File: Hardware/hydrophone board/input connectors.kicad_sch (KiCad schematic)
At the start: 9 parts, among them J202 Conn_01x02_Socket, J203 Screw_Terminal_01x02, J205 Conn_01x02_Socket, J207 Conn_01x02_Socket, J209 Conn_01x02_Socket

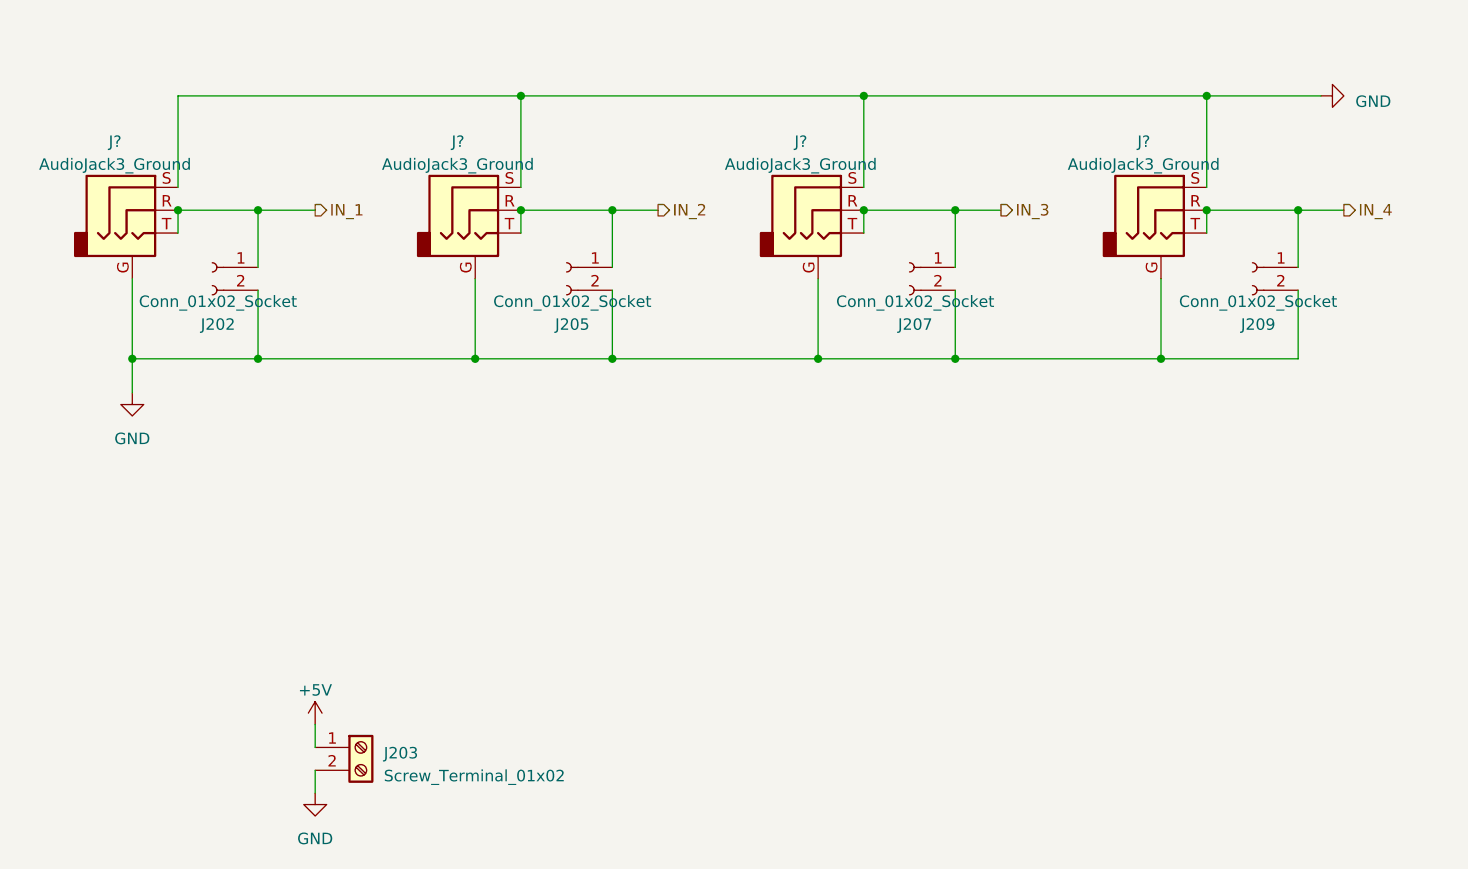
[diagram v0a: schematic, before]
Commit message: added teensy footprint
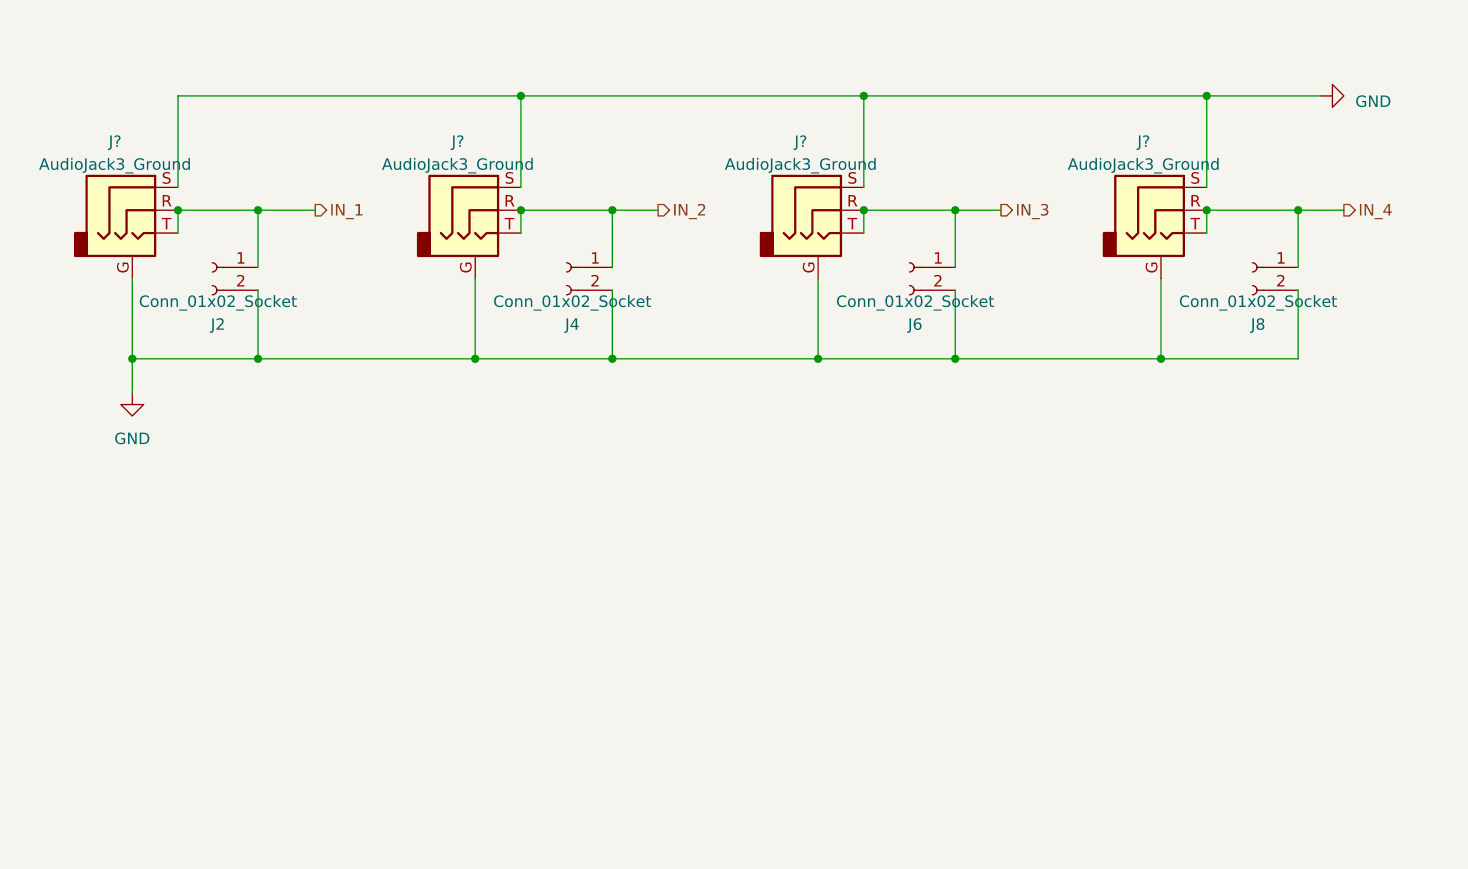
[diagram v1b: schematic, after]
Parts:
- removed J203: Screw_Terminal_01x02, symbol Connector:Screw_Terminal_01x02
- renumbered J202 to J2, J205 to J4, J207 to J6, J209 to J8
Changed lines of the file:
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@@
-    (stroke (width 0) (type default))
-  )
-  (wire (pts (xy 76.2 127) (xy 76.2 129.54))
     (stroke (width 0) (type default))
   )
@@
   )
   (wire (pts (xy 60.96 69.85) (xy 60.96 72.39))
-    (stroke (width 0) (type default))
-  )
-  (wire (pts (xy 76.2 132.08) (xy 76.2 134.62))
     (stroke (width 0) (type default))
   )
@@
         )
         (path "/4356d3a6-6a00-447d-897e-473f60221539/1cfbaf71-7039-4355-8fc7-d8c77f0e8058"
-          (reference "J201") (unit 1)
+          (reference "J1") (unit 1)
         )
       )
@@
   (symbol (lib_id "Connector:Conn_01x02_Socket") (at 180.34 76.2 0) (mirror y) (unit 1)
     (in_bom yes) (on_board yes) (dnp no)
-    (property "Reference" "J209" (at 180.975 82.55 0)
+    (property "Reference" "J8" (at 180.975 82.55 0)
       (effects (font (size 1.27 1.27)))
     )
@@
       (project "hydrophone board"
         (path "/4356d3a6-6a00-447d-897e-473f60221539/1cfbaf71-7039-4355-8fc7-d8c77f0e8058"
-          (reference "J209") (unit 1)
+          (reference "J8") (unit 1)
         )
       )
@@
         )
         (path "/4356d3a6-6a00-447d-897e-473f60221539/1cfbaf71-7039-4355-8fc7-d8c77f0e8058"
-          (reference "J204") (unit 1)
+          (reference "J3") (unit 1)
         )
       )
@@
   (symbol (lib_id "Connector:Conn_01x02_Socket") (at 142.24 76.2 0) (mirror y) (unit 1)
     (in_bom yes) (on_board yes) (dnp no)
-    (property "Reference" "J207" (at 142.875 82.55 0)
+    (property "Reference" "J6" (at 142.875 82.55 0)
       (effects (font (size 1.27 1.27)))
     )
@@
       (project "hydrophone board"
         (path "/4356d3a6-6a00-447d-897e-473f60221539/1cfbaf71-7039-4355-8fc7-d8c77f0e8058"
-          (reference "J207") (unit 1)
+          (reference "J6") (unit 1)
         )
       )
@@
         )
         (path "/4356d3a6-6a00-447d-897e-473f60221539/1cfbaf71-7039-4355-8fc7-d8c77f0e8058"
-          (reference "J206") (unit 1)
+          (reference "J5") (unit 1)
         )
       )
@@
   (symbol (lib_id "power:GND") (at 187.96 57.15 90) (unit 1)
     (in_bom yes) (on_board yes) (dnp no) (fields_autoplaced)
-    (property "Reference" "#PWR0203" (at 194.31 57.15 0)
+    (property "Reference" "#PWR02" (at 194.31 57.15 0)
       (effects (font (size 1.27 1.27)) hide)
     )
@@
       (project "hydrophone board"
         (path "/4356d3a6-6a00-447d-897e-473f60221539/1cfbaf71-7039-4355-8fc7-d8c77f0e8058"
-          (reference "#PWR0203") (unit 1)
-        )
-      )
-    )
-  )
-  (symbol (lib_id "Connector:Screw_Terminal_01x02") (at 81.28 129.54 0) (unit 1)
-    (in_bom yes) (on_board yes) (dnp no) (fields_autoplaced)
-    (property "Reference" "J203" (at 83.82 130.175 0)
-      (effects (font (size 1.27 1.27)) (justify left))
-    )
-    (property "Value" "Screw_Terminal_01x02" (at 83.82 132.715 0)
-      (effects (font (size 1.27 1.27)) (justify left))
-    )
-    (property "Footprint" "" (at 81.28 129.54 0)
-      (effects (font (size 1.27 1.27)) hide)
-    )
-    (property "Datasheet" "~" (at 81.28 129.54 0)
-      (effects (font (size 1.27 1.27)) hide)
-    )
-    (pin "1")
-    (pin "2")
-    (instances
-      (project "hydrophone board"
-        (path "/4356d3a6-6a00-447d-897e-473f60221539/1cfbaf71-7039-4355-8fc7-d8c77f0e8058"
-          (reference "J203") (unit 1)
-        )
-      )
-    )
-  )
-  (symbol (lib_id "power:GND") (at 76.2 134.62 0) (unit 1)
-    (in_bom yes) (on_board yes) (dnp no) (fields_autoplaced)
-    (property "Reference" "#PWR0201" (at 76.2 140.97 0)
-      (effects (font (size 1.27 1.27)) hide)
-    )
-    (property "Value" "GND" (at 76.2 139.7 0)
-      (effects (font (size 1.27 1.27)))
-    )
-    (property "Footprint" "" (at 76.2 134.62 0)
-      (effects (font (size 1.27 1.27)) hide)
-    )
-    (property "Datasheet" "" (at 76.2 134.62 0)
-      (effects (font (size 1.27 1.27)) hide)
-    )
-    (pin "1")
-    (instances
-      (project "hydrophone board"
-        (path "/4356d3a6-6a00-447d-897e-473f60221539/1cfbaf71-7039-4355-8fc7-d8c77f0e8058"
-          (reference "#PWR0201") (unit 1)
-        )
-      )
-    )
-  )
-  (symbol (lib_id "power:+5V") (at 76.2 127 0) (unit 1)
-    (in_bom yes) (on_board yes) (dnp no) (fields_autoplaced)
-    (property "Reference" "#PWR0202" (at 76.2 130.81 0)
-      (effects (font (size 1.27 1.27)) hide)
-    )
-    (property "Value" "+5V" (at 76.2 123.19 0)
-      (effects (font (size 1.27 1.27)))
-    )
-    (property "Footprint" "" (at 76.2 127 0)
-      (effects (font (size 1.27 1.27)) hide)
-    )
-    (property "Datasheet" "" (at 76.2 127 0)
-      (effects (font (size 1.27 1.27)) hide)
-    )
-    (pin "1")
-    (instances
-      (project "hydrophone board"
-        (path "/4356d3a6-6a00-447d-897e-473f60221539/1cfbaf71-7039-4355-8fc7-d8c77f0e8058"
-          (reference "#PWR0202") (unit 1)
+          (reference "#PWR02") (unit 1)
         )
       )
@@
         )
         (path "/4356d3a6-6a00-447d-897e-473f60221539/1cfbaf71-7039-4355-8fc7-d8c77f0e8058"
-          (reference "J208") (unit 1)
+          (reference "J7") (unit 1)
         )
       )
@@
   (symbol (lib_id "Connector:Conn_01x02_Socket") (at 64.77 76.2 0) (mirror y) (unit 1)
     (in_bom yes) (on_board yes) (dnp no)
-    (property "Reference" "J202" (at 65.405 82.55 0)
+    (property "Reference" "J2" (at 65.405 82.55 0)
       (effects (font (size 1.27 1.27)))
     )
@@
       (project "hydrophone board"
         (path "/4356d3a6-6a00-447d-897e-473f60221539/1cfbaf71-7039-4355-8fc7-d8c77f0e8058"
-          (reference "J202") (unit 1)
+          (reference "J2") (unit 1)
         )
       )
@@
   (symbol (lib_id "Connector:Conn_01x02_Socket") (at 104.14 76.2 0) (mirror y) (unit 1)
     (in_bom yes) (on_board yes) (dnp no)
-    (property "Reference" "J205" (at 104.775 82.55 0)
+    (property "Reference" "J4" (at 104.775 82.55 0)
       (effects (font (size 1.27 1.27)))
     )
@@
       (project "hydrophone board"
         (path "/4356d3a6-6a00-447d-897e-473f60221539/1cfbaf71-7039-4355-8fc7-d8c77f0e8058"
-          (reference "J205") (unit 1)
+          (reference "J4") (unit 1)
         )
       )
@@
   (symbol (lib_id "power:GND") (at 55.88 90.17 0) (unit 1)
     (in_bom yes) (on_board yes) (dnp no) (fields_autoplaced)
-    (property "Reference" "#PWR0205" (at 55.88 96.52 0)
+    (property "Reference" "#PWR01" (at 55.88 96.52 0)
       (effects (font (size 1.27 1.27)) hide)
     )
@@
       (project "hydrophone board"
         (path "/4356d3a6-6a00-447d-897e-473f60221539/1cfbaf71-7039-4355-8fc7-d8c77f0e8058"
-          (reference "#PWR0205") (unit 1)
-        )
-      )
+          (reference "#PWR01") (unit 1)
+        )
+      )

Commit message: changed connectors
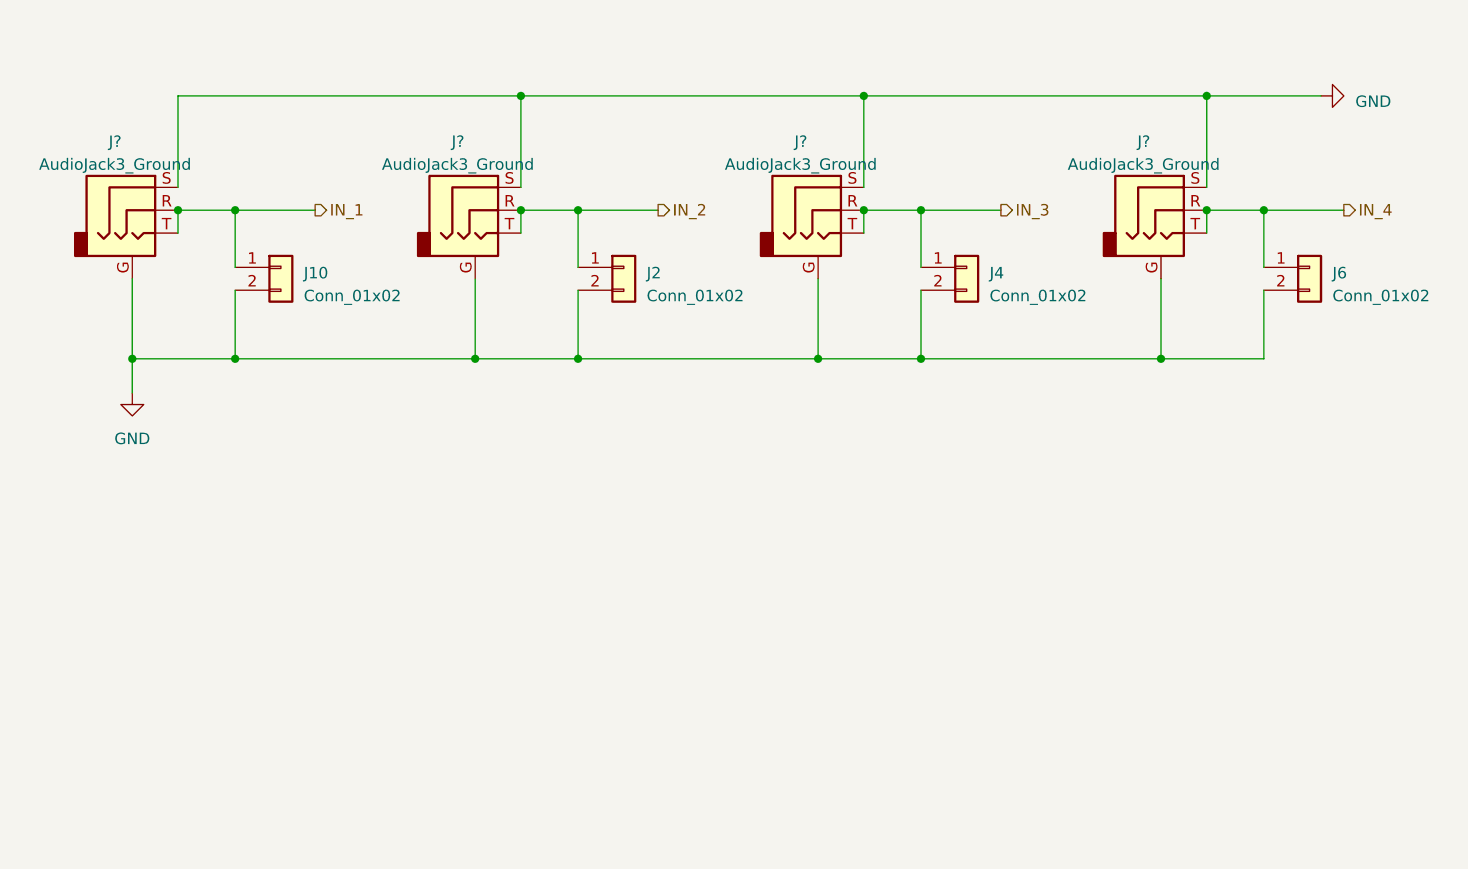
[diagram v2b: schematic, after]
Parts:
- removed J2, J4, J6, J8: Conn_01x02_Socket, symbol Connector:Conn_01x02_Socket
- added J10, J2, J4, J6: Conn_01x02, symbol Connector_Generic:Conn_01x02
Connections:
- net GND: now also J10.2 (Pin_2), J2.2 (Pin_2), J4.2 (Pin_2), J6.2 (Pin_2)
- net IN_1: now also J10.1 (Pin_1)
- net IN_2: now also J2.1 (Pin_1)
- net IN_3: now also J4.1 (Pin_1)
- net IN_4: now also J6.1 (Pin_1)

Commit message: annotate all component
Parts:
- renumbered J10 to J5, J2 to J6, J4 to J7, J6 to J8
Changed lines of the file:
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@@
   (symbol (lib_id "Connector_Generic:Conn_01x02") (at 110.49 76.2 0) (unit 1)
     (in_bom yes) (on_board yes) (dnp no) (fields_autoplaced)
-    (property "Reference" "J2" (at 113.03 76.835 0)
+    (property "Reference" "J6" (at 113.03 76.835 0)
       (effects (font (size 1.27 1.27)) (justify left))
     )
@@
       (project "hydrophone board"
         (path "/4356d3a6-6a00-447d-897e-473f60221539/1cfbaf71-7039-4355-8fc7-d8c77f0e8058"
-          (reference "J2") (unit 1)
+          (reference "J6") (unit 1)
         )
       )
@@
   (symbol (lib_id "Connector_Generic:Conn_01x02") (at 72.39 76.2 0) (unit 1)
     (in_bom yes) (on_board yes) (dnp no) (fields_autoplaced)
-    (property "Reference" "J10" (at 74.93 76.835 0)
+    (property "Reference" "J5" (at 74.93 76.835 0)
       (effects (font (size 1.27 1.27)) (justify left))
     )
@@
       (project "hydrophone board"
         (path "/4356d3a6-6a00-447d-897e-473f60221539/1cfbaf71-7039-4355-8fc7-d8c77f0e8058"
-          (reference "J10") (unit 1)
+          (reference "J5") (unit 1)
         )
       )
@@
         )
         (path "/4356d3a6-6a00-447d-897e-473f60221539/1cfbaf71-7039-4355-8fc7-d8c77f0e8058"
-          (reference "J3") (unit 1)
+          (reference "J2") (unit 1)
         )
       )
@@
   (symbol (lib_id "Connector_Generic:Conn_01x02") (at 148.59 76.2 0) (unit 1)
     (in_bom yes) (on_board yes) (dnp no) (fields_autoplaced)
-    (property "Reference" "J4" (at 151.13 76.835 0)
+    (property "Reference" "J7" (at 151.13 76.835 0)
       (effects (font (size 1.27 1.27)) (justify left))
     )
@@
       (project "hydrophone board"
         (path "/4356d3a6-6a00-447d-897e-473f60221539/1cfbaf71-7039-4355-8fc7-d8c77f0e8058"
-          (reference "J4") (unit 1)
+          (reference "J7") (unit 1)
         )
       )
@@
         )
         (path "/4356d3a6-6a00-447d-897e-473f60221539/1cfbaf71-7039-4355-8fc7-d8c77f0e8058"
-          (reference "J5") (unit 1)
+          (reference "J3") (unit 1)
         )
       )
@@
   (symbol (lib_id "power:GND") (at 187.96 57.15 90) (unit 1)
     (in_bom yes) (on_board yes) (dnp no) (fields_autoplaced)
-    (property "Reference" "#PWR02" (at 194.31 57.15 0)
+    (property "Reference" "#PWR01" (at 194.31 57.15 0)
       (effects (font (size 1.27 1.27)) hide)
     )
@@
       (project "hydrophone board"
         (path "/4356d3a6-6a00-447d-897e-473f60221539/1cfbaf71-7039-4355-8fc7-d8c77f0e8058"
-          (reference "#PWR02") (unit 1)
+          (reference "#PWR01") (unit 1)
         )
       )
@@
         )
         (path "/4356d3a6-6a00-447d-897e-473f60221539/1cfbaf71-7039-4355-8fc7-d8c77f0e8058"
-          (reference "J7") (unit 1)
+          (reference "J4") (unit 1)
         )
       )
@@
   (symbol (lib_id "Connector_Generic:Conn_01x02") (at 186.69 76.2 0) (unit 1)
     (in_bom yes) (on_board yes) (dnp no) (fields_autoplaced)
-    (property "Reference" "J6" (at 189.23 76.835 0)
+    (property "Reference" "J8" (at 189.23 76.835 0)
       (effects (font (size 1.27 1.27)) (justify left))
     )
@@
       (project "hydrophone board"
         (path "/4356d3a6-6a00-447d-897e-473f60221539/1cfbaf71-7039-4355-8fc7-d8c77f0e8058"
-          (reference "J6") (unit 1)
+          (reference "J8") (unit 1)
         )
       )
@@
   (symbol (lib_id "power:GND") (at 55.88 90.17 0) (unit 1)
     (in_bom yes) (on_board yes) (dnp no) (fields_autoplaced)
-    (property "Reference" "#PWR01" (at 55.88 96.52 0)
+    (property "Reference" "#PWR02" (at 55.88 96.52 0)
       (effects (font (size 1.27 1.27)) hide)
     )
@@
       (project "hydrophone board"
         (path "/4356d3a6-6a00-447d-897e-473f60221539/1cfbaf71-7039-4355-8fc7-d8c77f0e8058"
-          (reference "#PWR01") (unit 1)
-        )
-      )
+          (reference "#PWR02") (unit 1)
+        )
+      )
